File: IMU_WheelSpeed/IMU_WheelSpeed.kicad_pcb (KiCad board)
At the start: 2 copper layers, 23 parts, among them J1 Conn_01x06_Socket, J3 Conn_01x03_Socket, U1 PeripheralSOM, U2 LSM6DSL, U4 TPS71518__SC70

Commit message: random stitching vias
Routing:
- net (no net): vias 0 -> 73

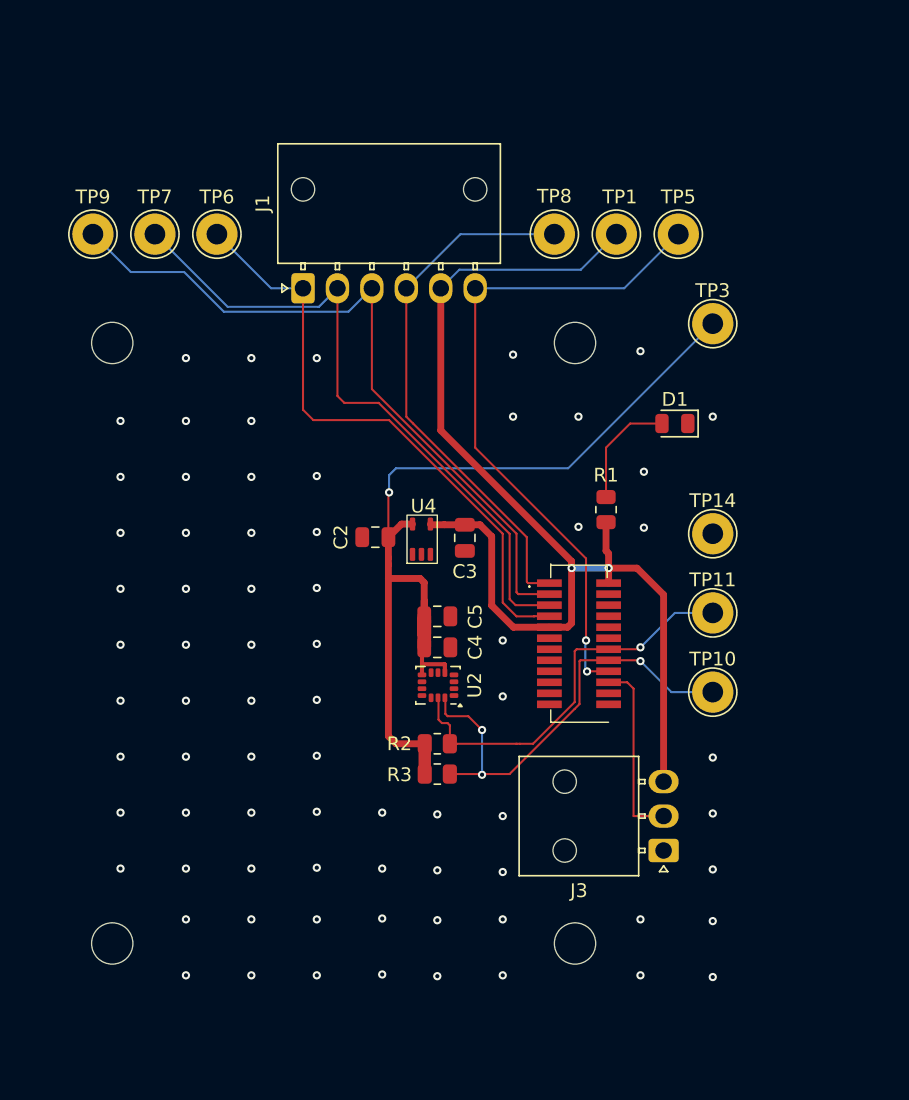
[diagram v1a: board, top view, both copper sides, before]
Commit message: (label "LDO_1.8V" (at 124.46 142.24 0) (fields_auteplaced yes)   (effects (font (size 0.762 0.762)) (justify left bottom)) (uuid "5df45f02-f0ff-424b-b1b0-8f9540b4e896") ) (label "LDO_1.8V" (at 124.46 142.24 0) (fields_autoplaced yes)   (effects (font (size 0.762 0.762)) (justify left bottom)) (uuid "5df45f02-f0ff-424b-b1b0-8f9540b4e896") )
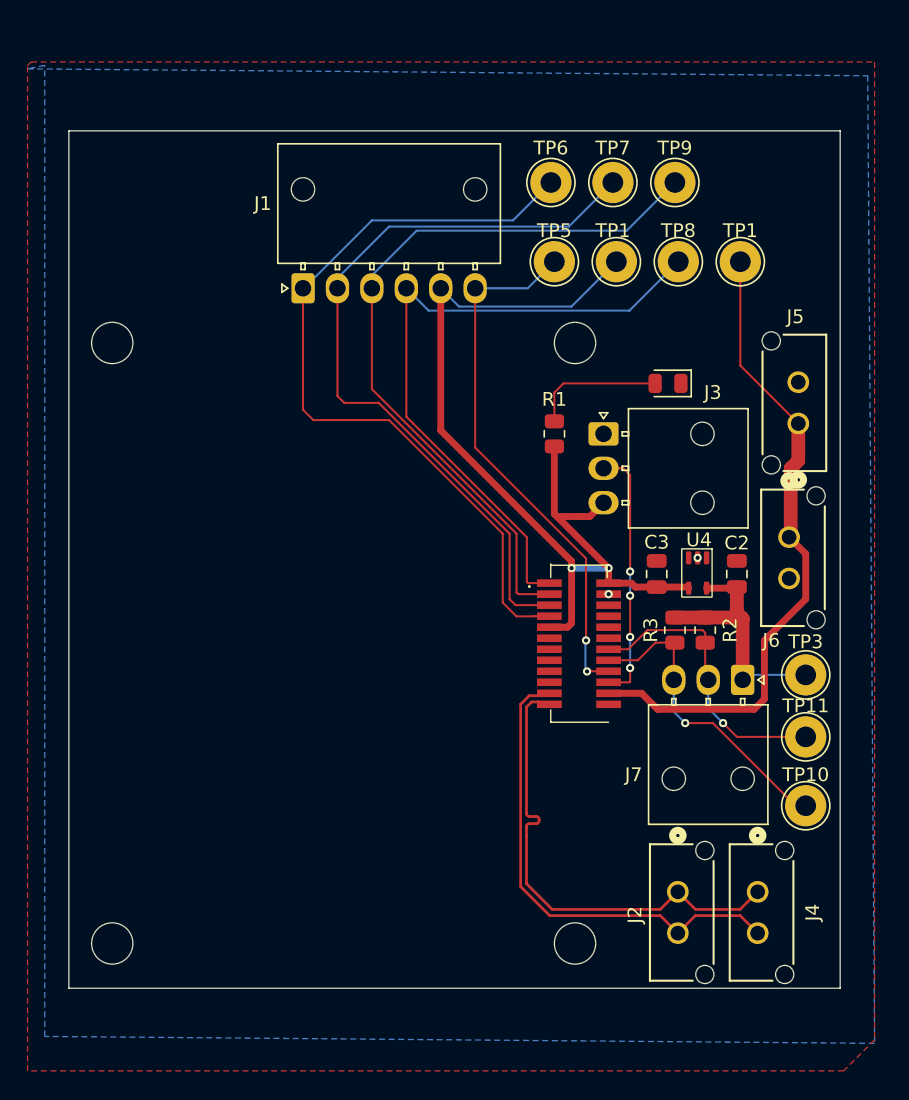
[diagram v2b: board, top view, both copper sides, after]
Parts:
- removed C4, C5: 100n, Capacitor_SMD:C_0805_2012Metric
- removed TP14: GND, TestPoint:TestPoint_THTPad_D3.0mm_Drill1.5mm
- removed U2: LSM6DSL, Package_LGA:LGA-14_3x2.5mm_P0.5mm_LayoutBorder3x4y
- added J2: CAN_IN, UTSVT_Connectors:CONN_SD-43650-006_02_MOL, F.Cu at (170.8, 107.2)
- added J4: CAN_OUT, UTSVT_Connectors:CONN_SD-43650-006_02_MOL, F.Cu at (176.5, 107.2)
- added J5: PWR_IN, UTSVT_Connectors:CONN_SD-43650-006_02_MOL, F.Cu at (178.9, 70.3)
- added J6: PWR_OUT, UTSVT_Connectors:CONN_SD-43650-006_02_MOL, F.Cu at (178.8, 81.5)
- added J7: Conn_01x03_Socket, Connector_Molex:Molex_Nano-Fit_105313-xx03_1x03_P2.50mm_Horizontal, F.Cu at (175.2, 90.4)
- added TP1: VDD, TestPoint:TestPoint_THTPad_D3.0mm_Drill1.5mm, F.Cu at (175.0, 60.0)
- TP3: value VDD -> LDO1.8V
- moved TP9 42.4 mm to (170.2, 54.2), turned to 90 degrees
- moved TP7 33.5 mm to (165.8, 54.2), turned to 90 degrees
- moved J3 30.6 mm to (165.1, 72.5), turned to 0 degrees
- moved U4 30.1 mm to (176.8, 82.7), turned to -90 degrees
- moved C2 26.4 mm to (174.8, 82.7), turned to 90 degrees
- moved TP3 26.4 mm to (179.8, 90.0)
- moved TP6 24.5 mm to (161.2, 54.2), turned to 90 degrees
- moved R2 21.1 mm to (172.4, 86.8), turned to 90 degrees
- moved R3 20.2 mm to (170.2, 86.8), turned to -90 degrees
- moved C3 14.2 mm to (168.9, 82.7), turned to 90 degrees
- moved TP11 11.2 mm to (179.8, 94.5), turned to -90 degrees
- moved TP10 10.7 mm to (179.8, 99.5), turned to -90 degrees
- moved TP5 9.22 mm to (161.5, 60.0), turned to -90 degrees
- moved TP8 9.22 mm to (170.5, 60.0), turned to -90 degrees
- moved R1 6.66 mm to (161.5, 72.5)
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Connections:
- net <NO NET> renamed GND
- R2 pad 1: /LDO_1.8V -> /IMU_I2C_SCL
- R2 pad 2: /IMU_I2C_SCL -> /LDO_1.8V
- U1 pad 21: unconnected-(U1-CAN_L-Pad21) -> /CAN_N
- U1 pad 22: unconnected-(U1-+12V_In-Pad22) -> /12V_IN
- U1 pad 23: unconnected-(U1-CAN_H-Pad23) -> /CAN_P
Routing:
- net /LDO_1.8V: track 68.4 -> 19.3 mm, vias 1 -> 0
- net /12V_IN: track 0.00 -> 47.6 mm
- net /CAN_N: track 0.00 -> 35.3 mm
- net /CAN_P: track 0.00 -> 35.3 mm
- net /VDD_3.3V: track 84.6 -> 68.9 mm
- net /MAG_CS: track 43.7 -> 57.0 mm
- net /IMU_I2C_SDA: track 32.9 -> 22.8 mm, vias 3 -> 1
- net /Mag_High: track 49.2 -> 39.4 mm
- net /MAGSLV_Input: track 39.0 -> 48.5 mm
- net /IMU_I2C_SCL: track 29.1 -> 21.2 mm
- net /MAG_CLK: track 48.3 -> 55.9 mm
- net /GPIO_1: track 13.4 -> 18.7 mm, vias 0 -> 4
- net /MAGSLV_Output: track 52.1 -> 54.6 mm
- net /LTE_D1: track 8.37 -> 9.67 mm
- net GND: vias 0 -> 2
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- added copper zone on B.Cu, net GND
- added copper zone on F.Cu, net GND
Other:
- board outline added: 56 x 62.2 mm

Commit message: Switched connectors
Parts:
- J1: footprint Connector_Molex:Molex_Nano-Fit_105313-xx06_1x06_P2.50mm_Horizontal -> UTSVT_Connectors:Molex_MicroFit_01x06_Horizontal
- J3, J7: footprint Connector_Molex:Molex_Nano-Fit_105313-xx03_1x03_P2.50mm_Horizontal -> UTSVT_Connectors:Molex_MicroFit3.0_1x3xP3.00mm_PolarizingPeg_Vertical
- moved TP9 40.8 mm to (129.8, 59.5), turned to -90 degrees
- moved TP7 31.9 mm to (134.2, 59.5), turned to -90 degrees
- moved TP6 27.0 mm to (134.2, 55.2), turned to -90 degrees
- moved TP10 24.4 mm to (169.2, 77.5)
- moved TP3 24.0 mm to (180.2, 66.0)
- moved J5 23.0 mm to (173.6, 92.7), turned to 180 degrees
- moved TP11 17.9 mm to (174.0, 77.5)
- moved J6 17.5 mm to (173.8, 98.2), turned to 180 degrees
- moved J3 12.5 mm to (177.5, 71.5), turned to 180 degrees
- moved J7 11.7 mm to (178.8, 79.2)
- moved J1 4.70 mm to (147.9, 61.3), turned to 180 degrees
- moved R2 3.47 mm to (169.0, 86.3)
- moved D1 2.54 mm to (168.0, 67.0), turned to -90 degrees
- moved R3 1.20 mm to (171.4, 86.3)
- moved C2 0.50 mm to (174.2, 82.7)
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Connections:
- J7 pad 2: /IMU_I2C_SCL -> /IMU_I2C_SDA
- J7 pad 3: /IMU_I2C_SDA -> /IMU_I2C_SCL
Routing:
- net /MAG_CLK: track 55.9 -> 11.1 mm
- net /12V_IN: track 47.6 -> 13.0 mm
- net /MAG_CS: track 57.0 -> 44.2 mm
- net /IMU_I2C_SDA: track 22.8 -> 32.9 mm
- net /VDD_3.3V: track 68.9 -> 77.6 mm
- net /GPIO_1: track 18.7 -> 27.0 mm
- net /LDO_1.8V: track 19.3 -> 26.6 mm
- net /MAGSLV_Output: track 54.6 -> 49.4 mm
- net /IMU_I2C_SCL: track 21.2 -> 25.4 mm, vias 1 -> 0
- net /MAGSLV_Input: track 48.5 -> 51.9 mm
- net /Mag_High: track 39.4 -> 40.2 mm
- net /LTE_D1: track 9.67 -> 9.15 mm
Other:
- board size 56 x 62.2 mm -> 56 x 61 mm

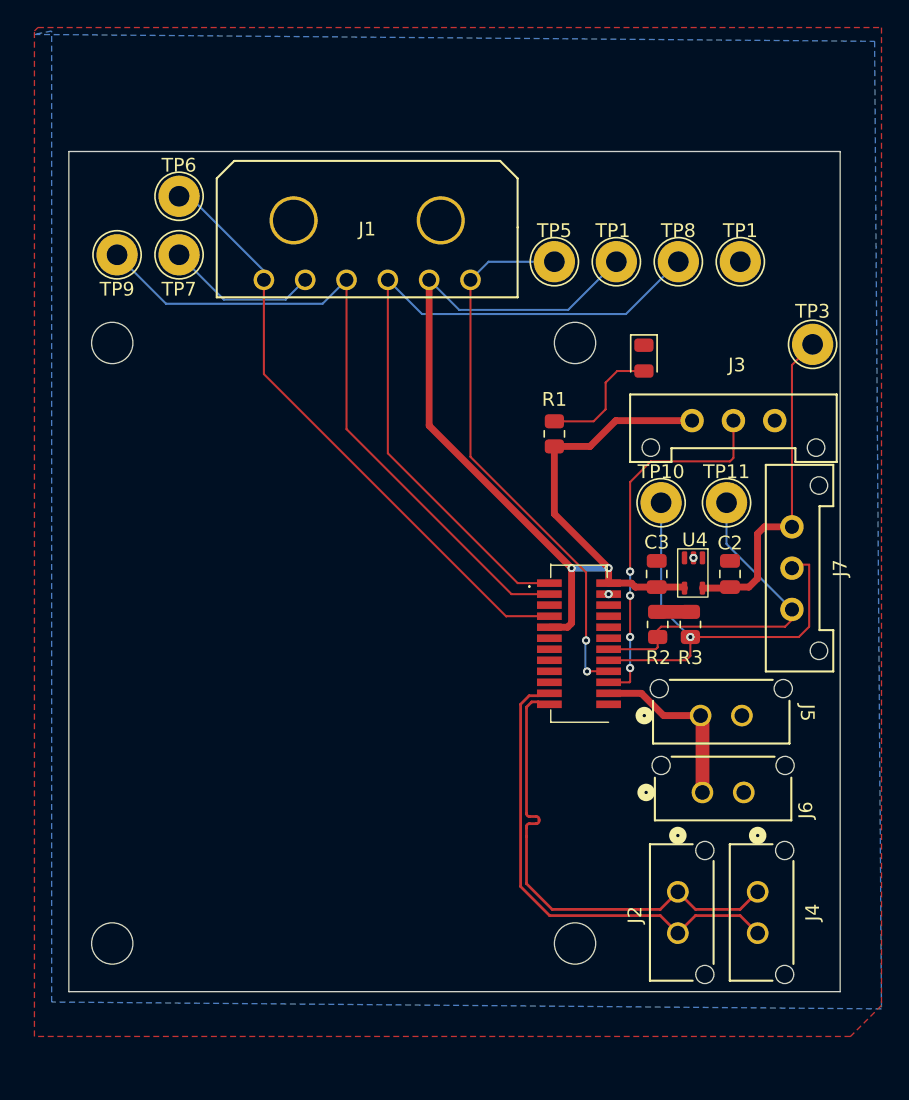
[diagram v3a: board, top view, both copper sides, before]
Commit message: Switched LDO Caps
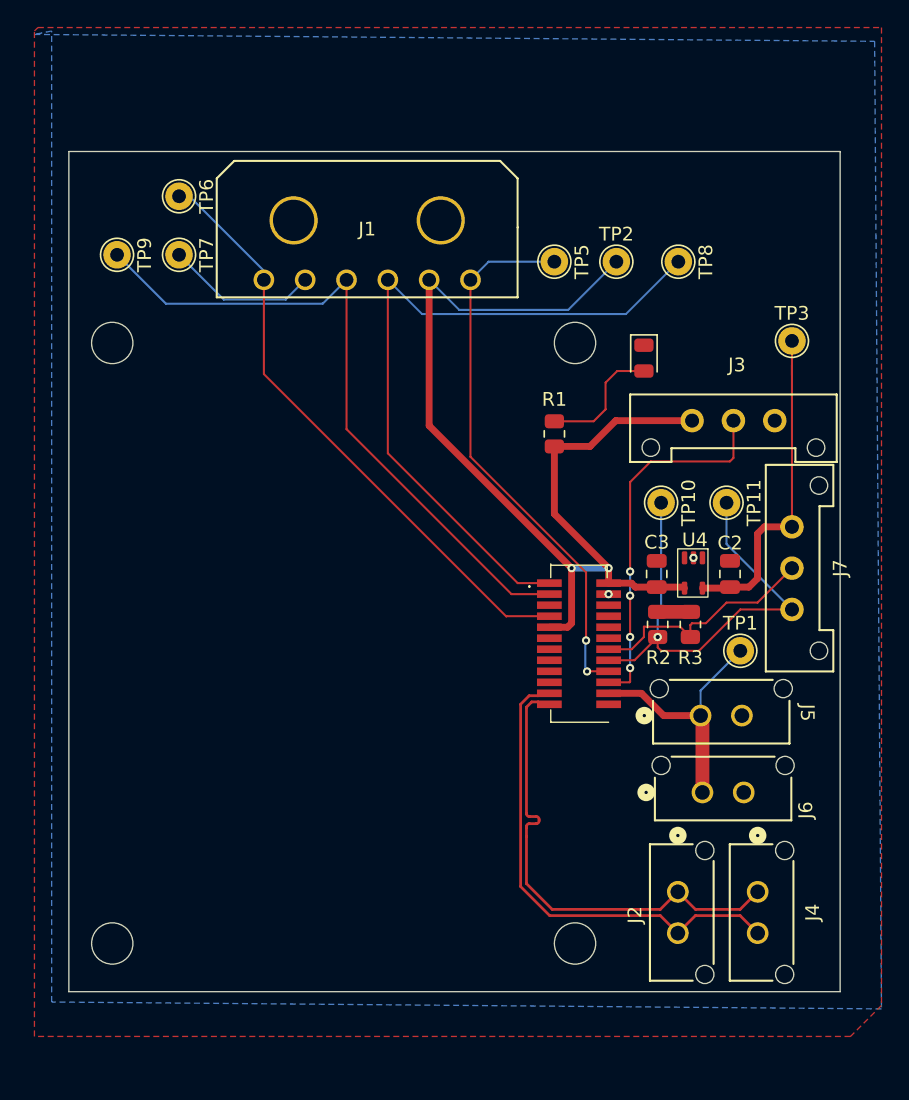
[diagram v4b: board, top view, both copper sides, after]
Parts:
- removed the TP1 at (166.0, 60.0)
- added TP2: VDD_3.3V, TestPoint:TestPoint_THTPad_D2.0mm_Drill1.0mm, F.Cu at (166.0, 60.0)
- TP1: value VDD -> 12V_IN; footprint TestPoint:TestPoint_THTPad_D3.0mm_Drill1.5mm -> TestPoint:TestPoint_THTPad_D2.0mm_Drill1.0mm
- TP10, TP11, TP3, TP5, TP6, TP7, TP8, TP9: footprint TestPoint:TestPoint_THTPad_D3.0mm_Drill1.5mm -> TestPoint:TestPoint_THTPad_D2.0mm_Drill1.0mm
- moved TP1 28.2 mm to (175.0, 88.2)
- moved TP3 1.52 mm to (178.8, 65.8)
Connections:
- J5 pad 1: /12V_IN -> +12V
- J6 pad 1: /12V_IN -> +12V
- J7 pad 2: /IMU_I2C_SDA -> /IMU_I2C_SCL
- J7 pad 3: /IMU_I2C_SCL -> /IMU_I2C_SDA
- R2 pad 1: /IMU_I2C_SCL -> /IMU_I2C_SDA
- R3 pad 2: /IMU_I2C_SDA -> /IMU_I2C_SCL
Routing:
- net /IMU_I2C_SDA: track 32.9 -> 26.0 mm
- net /12V_IN: track 13.0 -> 18.9 mm
- net /IMU_I2C_SCL: track 25.4 -> 27.0 mm

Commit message: Approved Connectors and gnd connected
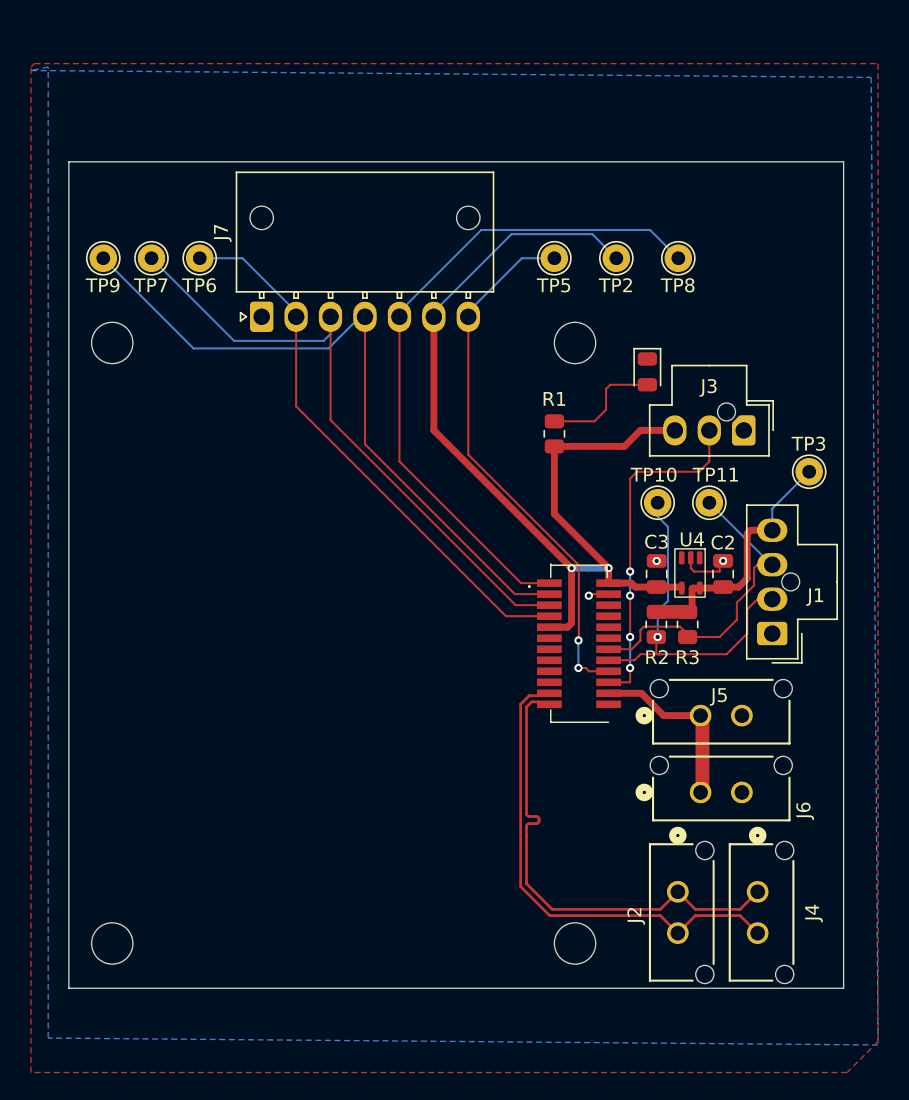
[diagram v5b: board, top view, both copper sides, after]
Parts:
- removed TP1: 12V_IN, TestPoint:TestPoint_THTPad_D2.0mm_Drill1.0mm
- C2: value 4u7 -> 0u47
- C3: value 4u7 -> 0u1
- J1: value Conn_01x06_Socket -> Conn_01x04_Socket; footprint UTSVT_Connectors:Molex_MicroFit_01x06_Horizontal -> Connector_Molex:Molex_Nano-Fit_105309-xx04_1x04_P2.50mm_Vertical
- J3: footprint UTSVT_Connectors:Molex_MicroFit3.0_1x3xP3.00mm_PolarizingPeg_Vertical -> Connector_Molex:Molex_Nano-Fit_105309-xx03_1x03_P2.50mm_Vertical
- J7: value Conn_01x03_Socket -> Conn_01x07_Socket; footprint UTSVT_Connectors:Molex_MicroFit3.0_1x3xP3.00mm_PolarizingPeg_Vertical -> Connector_Molex:Molex_Nano-Fit_105313-xx07_1x07_P2.50mm_Horizontal
- moved J7 41.4 mm to (140.2, 64.0), turned to 90 degrees
- moved J1 39.0 mm to (177.3, 87.0)
- moved TP3 9.58 mm to (180.0, 75.2)
- moved TP6 4.74 mm to (135.8, 59.8)
- moved J3 2.36 mm to (175.2, 72.2), turned to -90 degrees
- moved TP7 2.02 mm to (132.2, 59.8)
- moved TP11 1.25 mm to (172.8, 77.5)
- moved D1 1.03 mm to (168.2, 68.0)
- moved TP9 1.03 mm to (128.8, 59.8)
- moved C2 0.50 mm to (173.8, 82.7)
- moved TP10 0.25 mm to (169.0, 77.5)
- moved TP2 0.25 mm to (166.0, 59.8)
- moved TP5 0.25 mm to (161.5, 59.8)
- moved TP8 0.25 mm to (170.5, 59.8)
- moved U4 0.20 mm to (176.3, 82.7)
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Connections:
- J1 pad 1: /MAG_CS -> GND
- J1 pad 2: /MAG_CLK -> /IMU_I2C_SDA
- J1 pad 3: /MAGSLV_Output -> /IMU_I2C_SCL
- J1 pad 4: /MAGSLV_Input -> /LDO_1.8V
- J5 pad 1: +12V -> /12V_IN
- J6 pad 1: +12V -> /12V_IN
- J7 pad 1: /LDO_1.8V -> GND
- J7 pad 2: /IMU_I2C_SCL -> /MAG_CS
- J7 pad 3: /IMU_I2C_SDA -> /MAG_CLK
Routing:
- net /MAG_CLK: track 11.1 -> 46.3 mm
- net /LDO_1.8V: track 27.0 -> 19.2 mm
- net /12V_IN: track 18.9 -> 13.0 mm
- net GND: track 0.00 -> 5.32 mm, vias 2 -> 3
- net /MAG_CS: track 44.2 -> 40.2 mm
- net /VDD_3.3V: track 77.6 -> 73.7 mm
- net /IMU_I2C_SCL: track 27.0 -> 23.6 mm
- net /MAGSLV_Input: track 51.9 -> 49.0 mm
- net /GPIO_1: track 27.0 -> 24.8 mm
- net /MAGSLV_Output: track 49.4 -> 50.3 mm
- net /Mag_High: track 40.2 -> 39.4 mm
- net /IMU_I2C_SDA: track 26.0 -> 26.5 mm
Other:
- board size 56 x 61 mm -> 56.2 x 60 mm

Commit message: made cuter and added silkscreens
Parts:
- removed TP5: Mag_High, TestPoint:TestPoint_THTPad_D2.0mm_Drill1.0mm
- J7: value Conn_01x07_Socket -> Conn_01x06_Socket; footprint Connector_Molex:Molex_Nano-Fit_105313-xx07_1x07_P2.50mm_Horizontal -> Connector_Molex:Molex_Nano-Fit_105309-xx06_1x06_P2.50mm_Vertical
- moved J7 32.5 mm to (169.8, 77.5), turned to 180 degrees
- moved TP8 23.2 mm to (147.8, 64.2)
- moved TP6 22.9 mm to (158.2, 64.2)
- moved TP7 22.9 mm to (154.8, 64.2)
- moved TP9 22.9 mm to (151.2, 64.2)
- moved 3.3V 22.2 mm to (144.2, 64.2)
- moved IMU_SCL 20.8 mm to (181.0, 94.5)
- moved R1 18.2 mm to (179.7, 73.8), turned to 180 degrees
- moved IMU_SCL 15.4 mm to (181.0, 90.5)
- moved D1 11.9 mm to (179.7, 71.5), turned to 0 degrees
- moved J3 7.25 mm to (175.8, 65.0), turned to 90 degrees
- moved 1.8V 3.02 mm to (181.2, 78.0)
- moved 12V_IN 0.17 mm to (173.6, 98.4)
- renumbered TP3 to 1.8V, J6 to 12V_IN, TP2 to 3.3V, TP10 to IMU_SCL, TP11 to IMU_SCL
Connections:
- net /12V_IN renamed +12V
- J7 pad 1: GND -> /VDD_3.3V
- J7 pad 2: /MAG_CS -> /MAGSLV_Input
- J7 pad 3: /MAG_CLK -> /MAGSLV_Output
- J7 pad 4: /MAGSLV_Output -> /MAG_CLK
- J7 pad 5: /MAGSLV_Input -> /MAG_CS
- J7 pad 6: /VDD_3.3V -> GND
- U1 pad 18: /Mag_High -> unconnected-(U1-PA2(ADC)-Pad18)
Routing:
- net /Mag_High: track 39.4 -> 0.00 mm, vias 2 -> 0
- net /GPIO_1: track 24.8 -> 36.4 mm
- net /VDD_3.3V: track 73.7 -> 81.9 mm, vias 2 -> 1
- net /MAGSLV_Input: track 49.0 -> 55.8 mm, vias 0 -> 1
- net GND: track 5.32 -> 11.3 mm
- net /LTE_D1: track 8.73 -> 2.82 mm
- net /IMU_I2C_SCL: track 23.6 -> 29.0 mm
- net /MAG_CS: track 40.2 -> 43.5 mm, vias 0 -> 1
- net /MAG_CLK: track 46.3 -> 43.8 mm, vias 0 -> 1
- net /IMU_I2C_SDA: track 26.5 -> 28.7 mm, vias 1 -> 0
- net /LDO_1.8V: track 19.2 -> 18.4 mm
- net /MAGSLV_Output: track 50.3 -> 49.6 mm, vias 0 -> 1
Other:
- board size 56.2 x 60 mm -> 56.8 x 50 mm
- board text added: "12V_OUT"
- board text added: "CAN IN"
- board text added: "CAN OUT"
- board text added: "HALL_E_CONN"
- board text added: "IMU_CONN"
- board text added: "LIN_POT_CONN"
- board text added: "MG_CLK"
- board text added: "MG_CS"
- board text added: "MG_SLV_IN"
- board text added: "MG_SLV_OUT"

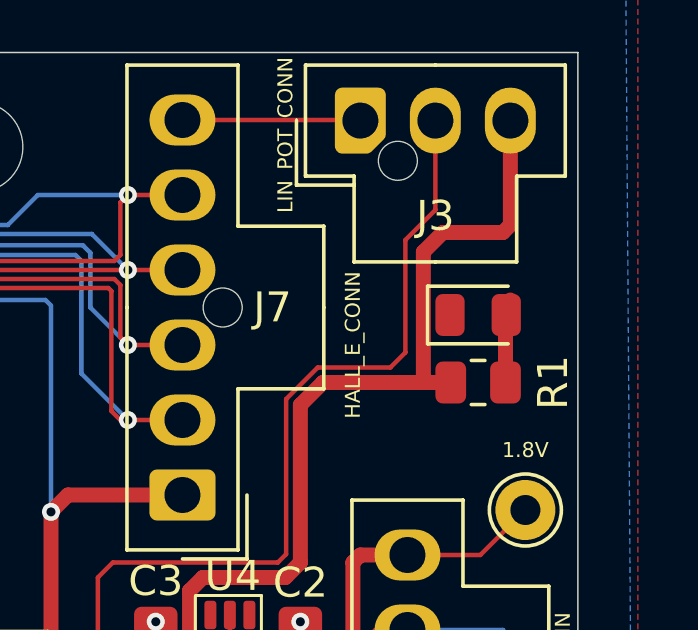
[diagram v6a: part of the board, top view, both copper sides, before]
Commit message: 3d Models added
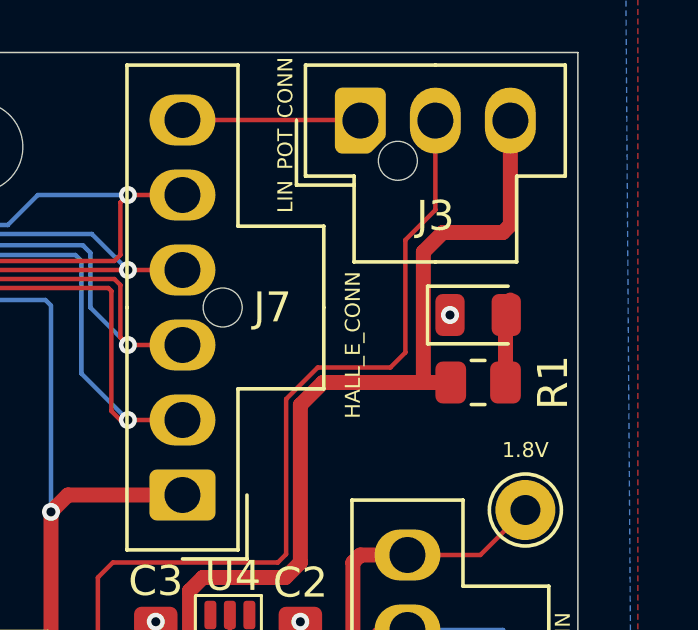
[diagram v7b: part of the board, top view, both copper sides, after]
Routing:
- net GND: vias 3 -> 4
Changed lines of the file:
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@@
+		(net 25)
+	)
+	(via
+		(at 178.7375 71.5)
+		(size 0.6)
+		(drill 0.3)
+		(layers "F.Cu" "B.Cu")
 		(net 25)
 	)
